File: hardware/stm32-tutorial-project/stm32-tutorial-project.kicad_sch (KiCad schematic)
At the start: 20 parts, among them SW1 SW_Push, U1 STM32G431CBTx

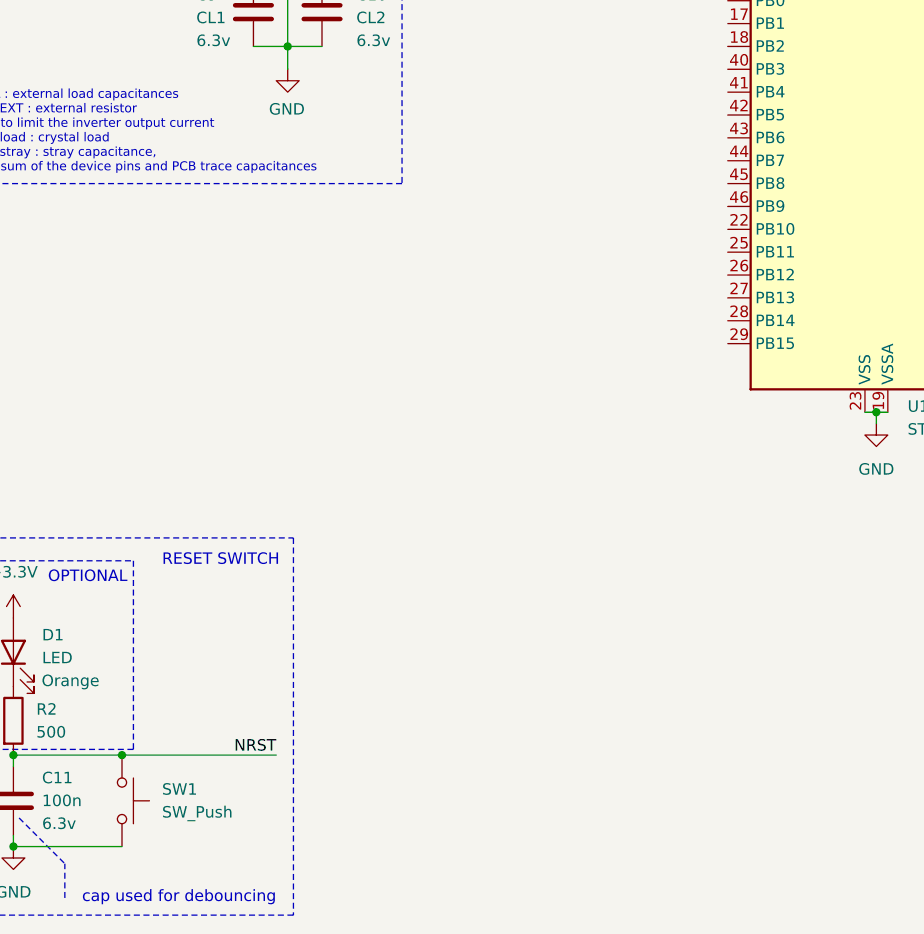
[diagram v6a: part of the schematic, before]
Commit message: added boot mode switch
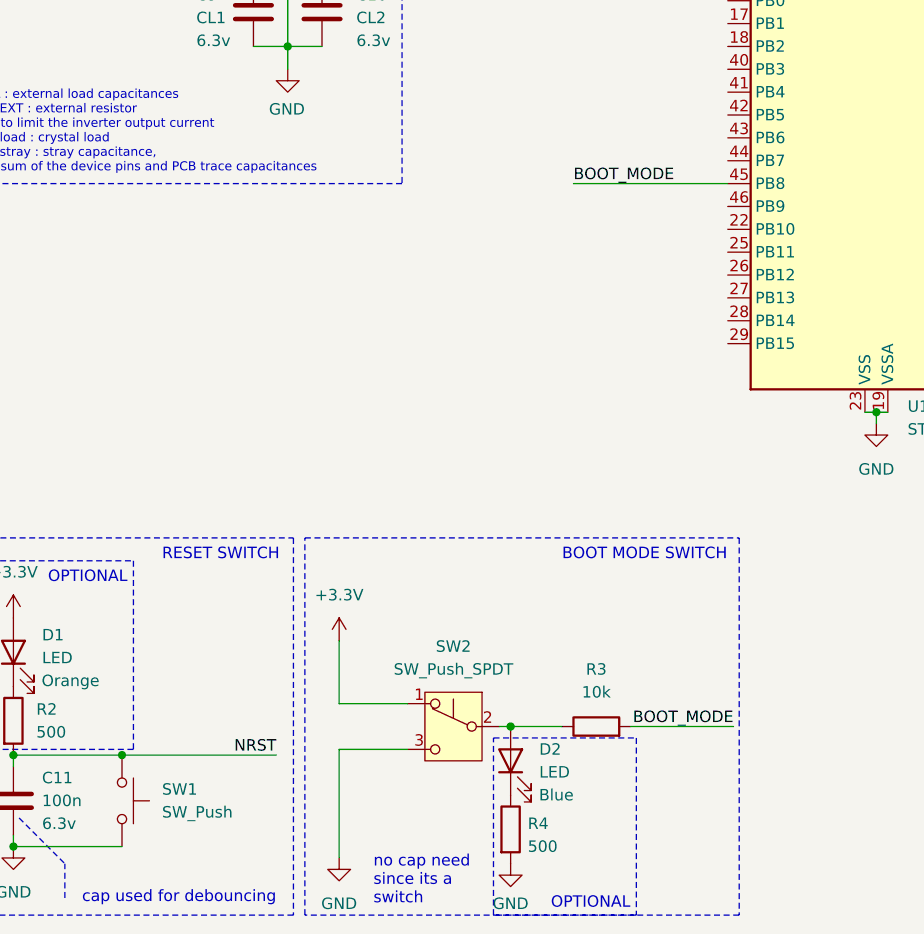
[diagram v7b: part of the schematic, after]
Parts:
- added D2: LED, symbol Device:LED
- added R3: 10k, symbol Device:R
- added R4: 500, symbol Device:R
- added SW2: SW_Push_SPDT, symbol Switch:SW_Push_SPDT
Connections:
- net +3.3V: now also SW2.1 (A)
- net GND: now also R4.2, SW2.3 (C)
- net BOOT_MODE: now reaches U1.45 (PB8)
- net BOOT_MODE: now also R3.2
- new net: D2.2 (A), R3.1, SW2.2 (B)
- new net: D2.1 (K), R4.1
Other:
- note added: "BOOT MODE SWITCH"
- note added: "no cap need since its a switch"

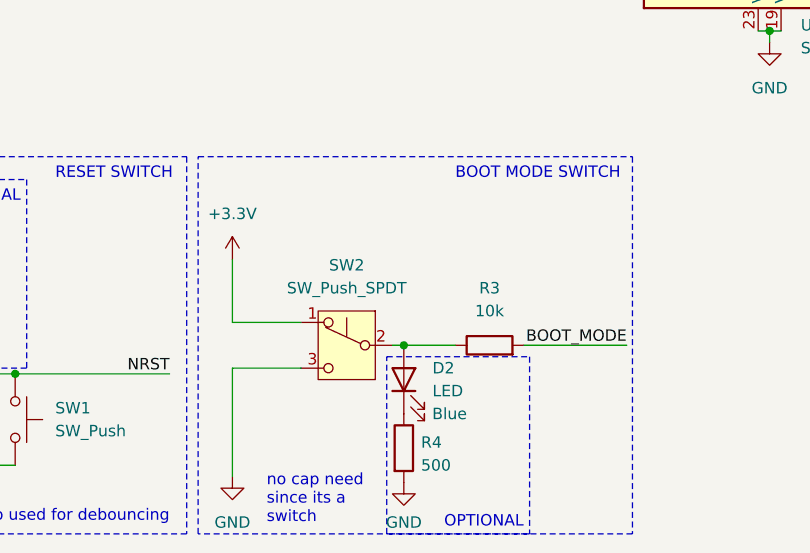
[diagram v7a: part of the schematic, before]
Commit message: added boot mode switch
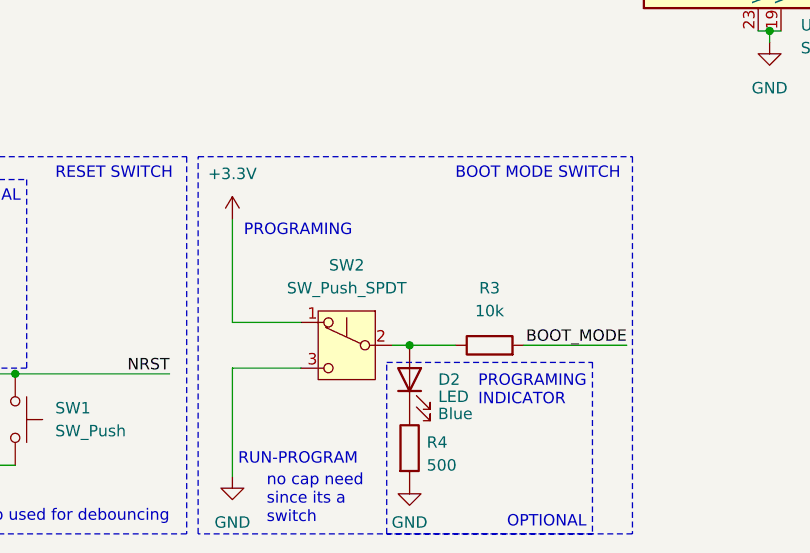
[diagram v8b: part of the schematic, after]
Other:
- note added: "PROGRAMING"
- note added: "PROGRAMING INDICATOR"
- note added: "RUN-PROGRAM"
- moved on the sheet: D2, R4
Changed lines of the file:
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@@
 	)
 	(junction
+		(at 75.565 174.625)
+		(diameter 0)
+		(color 0 0 0 0)
+	)
+	(junction
 		(at 136.525 53.975)
 		(diameter 0)
@@
 	)
 	(junction
-		(at 74.93 174.625)
-		(diameter 0)
-		(color 0 0 0 0)
-	)
-	(junction
 		(at 53.975 86.995)
 		(diameter 0)
@@
 	(wire
 		(pts
-			(xy 55.88 165.1) (xy 55.88 172.085)
+			(xy 55.88 160.655) (xy 55.88 172.085)
 		)
 		(stroke
@@
 	(wire
 		(pts
-			(xy 80.645 174.625) (xy 74.93 174.625)
+			(xy 80.645 174.625) (xy 75.565 174.625)
 		)
 		(stroke
@@
 	(wire
 		(pts
-			(xy 74.93 174.625) (xy 73.66 174.625)
+			(xy 31.75 177.8) (xy 48.895 177.8)
 		)
 		(stroke
@@
 	(wire
 		(pts
-			(xy 31.75 177.8) (xy 48.895 177.8)
+			(xy 59.69 45.085) (xy 59.69 46.355)
 		)
 		(stroke
@@
 	(wire
 		(pts
-			(xy 59.69 45.085) (xy 59.69 46.355)
+			(xy 73.66 174.625) (xy 75.565 174.625)
 		)
 		(stroke
@@
 	)
 	(rectangle
-		(start 73.025 175.895)
-		(end 88.9 195.58)
+		(start 73.025 176.53)
+		(end 95.885 195.58)
 		(stroke
 			(width 0)
@@
 		)
 	)
+	(text "PROGRAMING\nINDICATOR"
+		(exclude_from_sim no)
+		(at 83.185 179.705 0)
+		(effects
+			(font
+				(size 1.27 1.27)
+			)
+			(justify left)
+		)
+	)
 	(text "stm32g431cb-1 datasheet 5.1.6 Power supply scheme p.g. 68"
 		(exclude_from_sim no)
@@
 		)
 	)
+	(text "PROGRAMING"
+		(exclude_from_sim no)
+		(at 57.15 161.925 0)
+		(effects
+			(font
+				(size 1.27 1.27)
+			)
+			(justify left)
+		)
+	)
 	(text "1.55 - 3.6 V"
 		(exclude_from_sim no)
@@
 		)
 	)
+	(text "RUN-PROGRAM"
+		(exclude_from_sim no)
+		(at 56.515 187.325 0)
+		(effects
+			(font
+				(size 1.27 1.27)
+			)
+			(justify left)
+		)
+	)
 	(text "CL : external load capacitances\nR_EXT : external resistor \n	to limit the inverter output current\nC_load : crystal load\nC_stray : stray capacitance, \n	sum of the device pins and PCB trace capacitances"
 		(exclude_from_sim no)
@@
 	(text "OPTIONAL"
 		(exclude_from_sim no)
-		(at 83.82 194.31 0)
+		(at 90.805 194.31 0)
 		(effects
 			(font
@@
 	(symbol
 		(lib_id "power:+3.3V")
-		(at 55.88 165.1 0)
+		(at 55.88 160.655 0)
 		(unit 1)
 		(exclude_from_sim no)
@@
 		(fields_autoplaced yes)
 		(property "Reference" "#PWR013"
-			(at 55.88 168.91 0)
+			(at 55.88 164.465 0)
 			(effects
 				(font
@@
 		)
 		(property "Value" "+3.3V"
-			(at 55.88 160.02 0)
+			(at 55.88 155.575 0)
 			(effects
 				(font
@@
 		)
 		(property "Footprint" ""
-			(at 55.88 165.1 0)
+			(at 55.88 160.655 0)
 			(effects
 				(font
@@
 		)
 		(property "Datasheet" ""
-			(at 55.88 165.1 0)
+			(at 55.88 160.655 0)
 			(effects
 				(font
@@
 		)
 		(property "Description" "Power symbol creates a global label with name \"+3.3V\""
-			(at 55.88 165.1 0)
+			(at 55.88 160.655 0)
 			(effects
 				(font
@@
 	(symbol
 		(lib_id "Device:R")
-		(at 74.93 186.055 0)
+		(at 75.565 186.055 0)
 		(unit 1)
 		(exclude_from_sim no)
@@
 		(dnp no)
 		(property "Reference" "R4"
-			(at 76.835 185.42 0)
+			(at 77.47 185.42 0)
 			(effects
 				(font
@@
 		)
 		(property "Value" "500"
-			(at 76.835 187.96 0)
+			(at 77.47 187.96 0)
 			(effects
 				(font
@@
 		)
 		(property "Footprint" ""
-			(at 73.152 186.055 90)
+			(at 73.787 186.055 90)
 			(effects
 				(font
@@
 		)
 		(property "Datasheet" "~"
-			(at 74.93 186.055 0)
+			(at 75.565 186.055 0)
 			(effects
 				(font
@@
 		)
 		(property "Description" "Resistor"
-			(at 74.93 186.055 0)
+			(at 75.565 186.055 0)
 			(effects
 				(font
@@
 	(symbol
 		(lib_id "power:GND")
-		(at 74.93 189.865 0)
+		(at 75.565 189.865 0)
 		(unit 1)
 		(exclude_from_sim no)
@@
 		(dnp no)
 		(property "Reference" "#PWR015"
-			(at 74.93 196.215 0)
+			(at 75.565 196.215 0)
 			(effects
 				(font
@@
 		)
 		(property "Value" "GND"
-			(at 74.93 194.31 0)
+			(at 75.565 194.31 0)
 			(effects
 				(font
@@
 		)
 		(property "Footprint" ""
-			(at 74.93 189.865 0)
+			(at 75.565 189.865 0)
 			(effects
 				(font
@@
 		)
 		(property "Datasheet" ""
-			(at 74.93 189.865 0)
+			(at 75.565 189.865 0)
 			(effects
 				(font
@@
 		)
 		(property "Description" "Power symbol creates a global label with name \"GND\" , ground"
-			(at 74.93 189.865 0)
+			(at 75.565 189.865 0)
 			(effects
 				(font
@@
 	(symbol
 		(lib_id "Device:LED")
-		(at 74.93 178.435 90)
+		(at 75.565 178.435 90)
 		(unit 1)
 		(exclude_from_sim no)
@@
 		(dnp no)
 		(property "Reference" "D2"
-			(at 78.105 177.165 90)
+			(at 78.74 178.435 90)
 			(effects
 				(font
@@
 		)
 		(property "Value" "LED"
-			(at 78.105 179.705 90)
+			(at 78.74 180.34 90)
 			(effects
 				(font
@@
 		)
 		(property "Footprint" ""
-			(at 74.93 178.435 0)
+			(at 75.565 178.435 0)
 			(effects
 				(font
@@
 		)
 		(property "Datasheet" "~"
-			(at 74.93 178.435 0)
+			(at 75.565 178.435 0)
 			(effects
 				(font
@@
 		)
 		(property "Description" "Light emitting diode"
-			(at 74.93 178.435 0)
+			(at 75.565 178.435 0)
 			(effects
 				(font
@@
 		)
 		(property "Colour" "Blue"
-			(at 80.01 182.245 90)
+			(at 80.645 182.245 90)
 			(effects
 				(font
